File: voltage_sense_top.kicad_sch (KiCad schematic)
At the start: 46 parts, among them IC1 DAC101C081CIMK_NOPB, J1 Conn_Coaxial, J2 Conn_01x04, J4 HDMI_A, J5 Conn_Coaxial, U1 OPA188xxDBV, U2 ADA4000-1, U3 OPA188xxDBV, U4 MCP4017T-103E_LT, U5 OPA1641

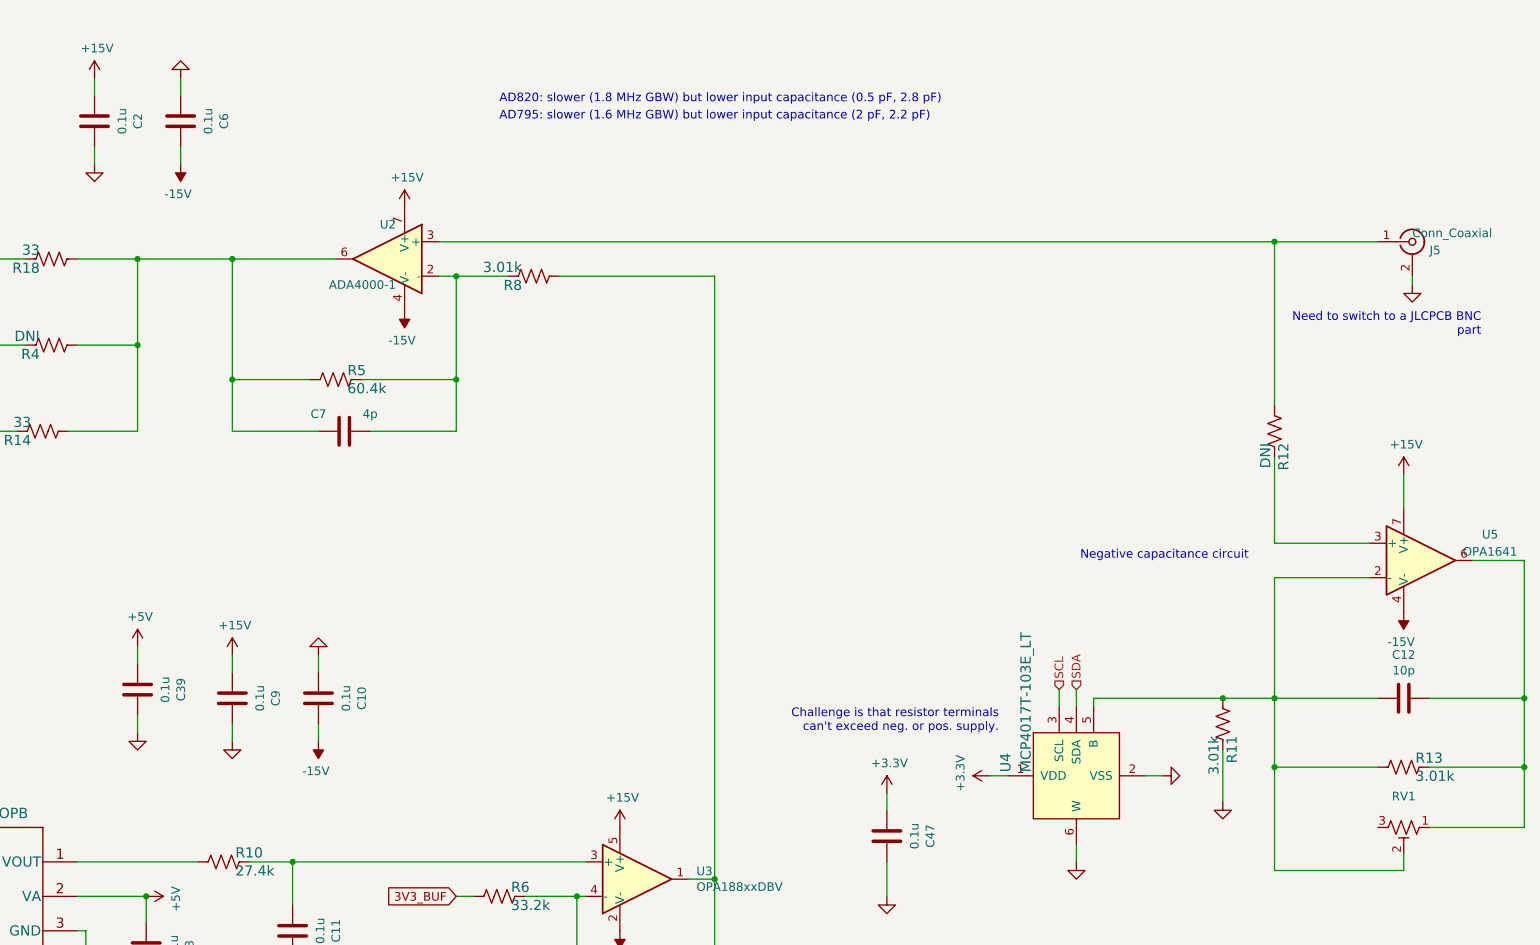
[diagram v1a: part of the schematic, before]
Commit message: moved SMA to same size as HDMI
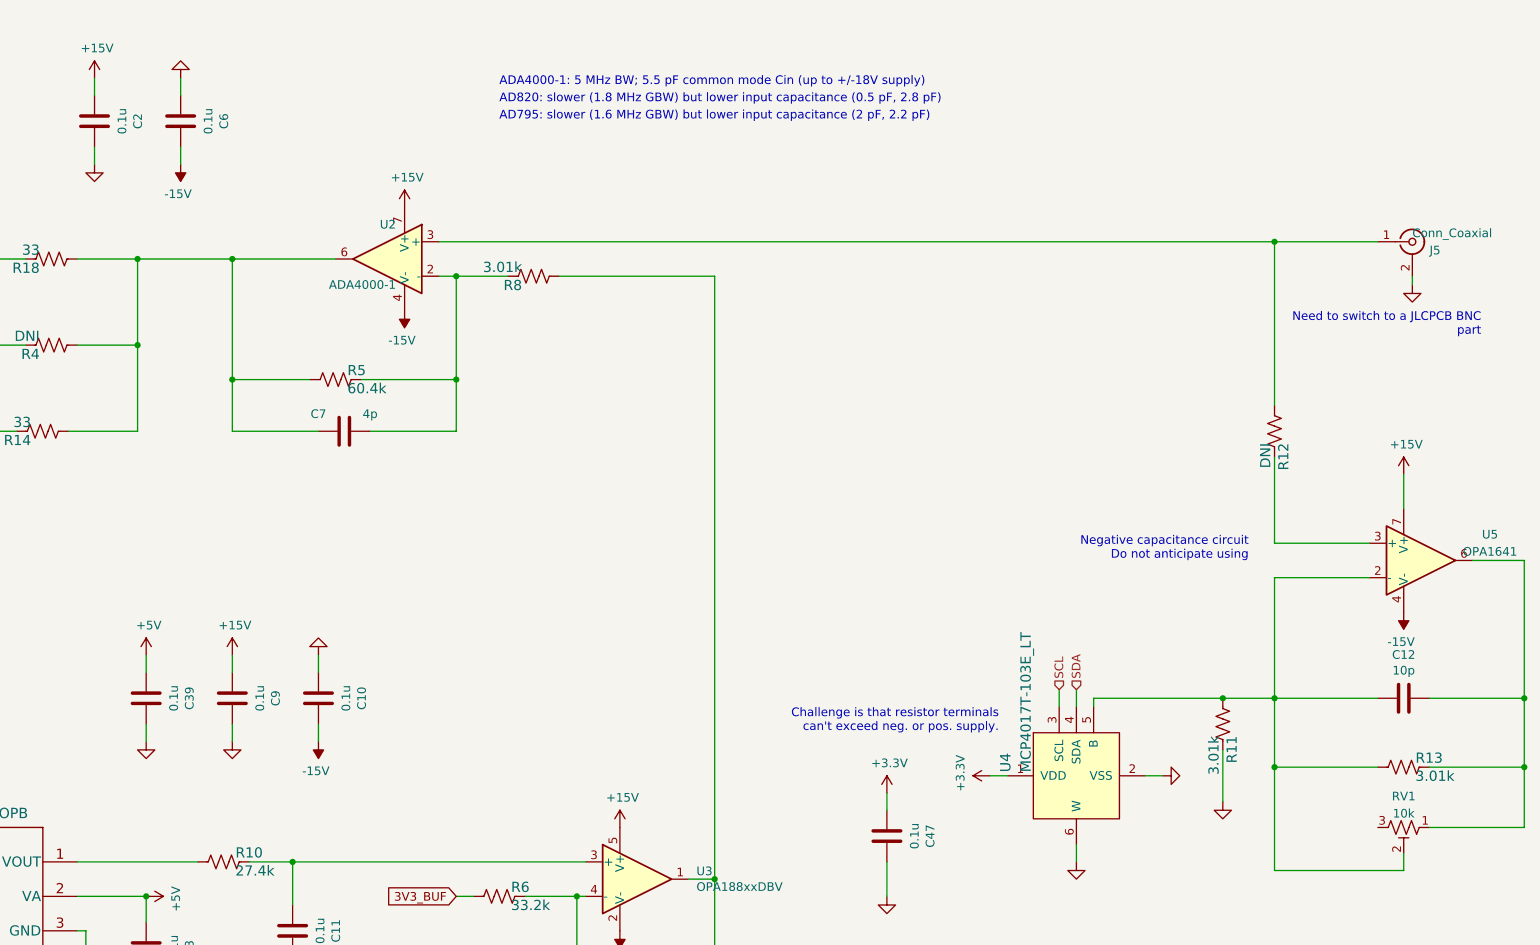
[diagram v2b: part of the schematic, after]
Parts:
- RV1: value (none) -> 10k; footprint (none) -> covg-kicad:Potentiometer_Nidec_ST-5ETW
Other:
- note added: "ADA4000-1: 5 MHz BW; 5.5 pF common mode Cin (up to +/-18V supply)"
- note added: "Negative capacitance circuit Do not anticipate using"
- note removed: "Negative capacitance circuit"
- moved on the sheet: C39
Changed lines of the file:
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@@
     (stroke (width 0) (type default) (color 0 0 0 0))
   )
-  (wire (pts (xy 199.39 119.38) (xy 199.39 116.84))
+  (wire (pts (xy 200.66 120.65) (xy 200.66 118.11))
     (stroke (width 0) (type default) (color 0 0 0 0))
   )
@@
     (stroke (width 0) (type default) (color 0 0 0 0))
   )
-  (wire (pts (xy 199.39 109.22) (xy 199.39 106.68))
+  (wire (pts (xy 200.66 110.49) (xy 200.66 107.95))
     (stroke (width 0) (type default) (color 0 0 0 0))
   )
@@
     (effects (font (size 1.27 1.27)) (justify left bottom))
   )
-  (text "Negative capacitance circuit" (at 363.22 93.98 180)
+  (text "Negative capacitance circuit\nDo not anticipate using"
+    (at 363.22 93.98 0)
     (effects (font (size 1.27 1.27)) (justify right bottom))
   )
@@
     (effects (font (size 1.27 1.27)) (justify right bottom))
   )
+  (text "ADA4000-1: 5 MHz BW; 5.5 pF common mode Cin (up to +/-18V supply) "
+    (at 252.73 24.13 0)
+    (effects (font (size 1.27 1.27)) (justify left bottom))
+  )
   (label "SDA" (at 140.97 148.59 0)
     (effects (font (size 1.27 1.27)) (justify left bottom))
@@
     (pin "2")
   )
-  (symbol (lib_id "Device:C") (at 199.39 113.03 180) (unit 1)
-    (in_bom yes) (on_board yes)
-    (property "Reference" "C39" (id 0) (at 205.7908 113.03 90))
-    (property "Value" "0.1u" (id 1) (at 203.4794 113.03 90))
-    (property "Footprint" "Capacitor_SMD:C_0603_1608Metric" (id 2) (at 198.4248 109.22 0)
-      (effects (font (size 1.27 1.27)) hide)
-    )
-    (property "Datasheet" "~" (id 3) (at 199.39 113.03 0)
-      (effects (font (size 1.27 1.27)) hide)
-    )
-    (property "Manf#" "CC0603MRX7R8BB104" (id 4) (at 205.7908 115.57 0)
-      (effects (font (size 1.27 1.27)) hide)
-    )
-    (property "Tolerance" "20%" (id 5) (at 205.7908 115.57 0)
-      (effects (font (size 1.27 1.27)) hide)
-    )
-    (property "voltage" "25V" (id 6) (at 205.7908 115.57 0)
-      (effects (font (size 1.27 1.27)) hide)
-    )
-    (pin "1")
-    (pin "2")
-  )
-  (symbol (lib_id "power:GND") (at 199.39 119.38 0) (unit 1)
-    (in_bom yes) (on_board yes)
-    (property "Reference" "#PWR0184" (id 0) (at 199.39 125.73 0)
-      (effects (font (size 1.27 1.27)) hide)
-    )
-    (property "Value" "GND" (id 1) (at 199.517 122.6312 90)
+  (symbol (lib_id "Device:C") (at 200.66 114.3 180) (unit 1)
+    (in_bom yes) (on_board yes)
+    (property "Reference" "C39" (id 0) (at 207.0608 114.3 90))
+    (property "Value" "0.1u" (id 1) (at 204.7494 114.3 90))
+    (property "Footprint" "Capacitor_SMD:C_0603_1608Metric" (id 2) (at 199.6948 110.49 0)
+      (effects (font (size 1.27 1.27)) hide)
+    )
+    (property "Datasheet" "~" (id 3) (at 200.66 114.3 0)
+      (effects (font (size 1.27 1.27)) hide)
+    )
+    (property "Manf#" "CC0603MRX7R8BB104" (id 4) (at 207.0608 116.84 0)
+      (effects (font (size 1.27 1.27)) hide)
+    )
+    (property "Tolerance" "20%" (id 5) (at 207.0608 116.84 0)
+      (effects (font (size 1.27 1.27)) hide)
+    )
+    (property "voltage" "25V" (id 6) (at 207.0608 116.84 0)
+      (effects (font (size 1.27 1.27)) hide)
+    )
+    (pin "1")
+    (pin "2")
+  )
+  (symbol (lib_id "power:GND") (at 200.66 120.65 0) (unit 1)
+    (in_bom yes) (on_board yes)
+    (property "Reference" "#PWR0184" (id 0) (at 200.66 127 0)
+      (effects (font (size 1.27 1.27)) hide)
+    )
+    (property "Value" "GND" (id 1) (at 200.787 123.9012 90)
       (effects (font (size 1.27 1.27)) (justify right) hide)
     )
-    (property "Footprint" "" (id 2) (at 199.39 119.38 0)
-      (effects (font (size 1.27 1.27)) hide)
-    )
-    (property "Datasheet" "" (id 3) (at 199.39 119.38 0)
-      (effects (font (size 1.27 1.27)) hide)
-    )
-    (pin "1")
-  )
-  (symbol (lib_id "power:+5V") (at 199.39 106.68 0) (unit 1)
-    (in_bom yes) (on_board yes)
-    (property "Reference" "#PWR0186" (id 0) (at 199.39 110.49 0)
-      (effects (font (size 1.27 1.27)) hide)
-    )
-    (property "Value" "+5V" (id 1) (at 199.771 102.2858 0))
-    (property "Footprint" "" (id 2) (at 199.39 106.68 0)
-      (effects (font (size 1.27 1.27)) hide)
-    )
-    (property "Datasheet" "" (id 3) (at 199.39 106.68 0)
+    (property "Footprint" "" (id 2) (at 200.66 120.65 0)
+      (effects (font (size 1.27 1.27)) hide)
+    )
+    (property "Datasheet" "" (id 3) (at 200.66 120.65 0)
+      (effects (font (size 1.27 1.27)) hide)
+    )
+    (pin "1")
+  )
+  (symbol (lib_id "power:+5V") (at 200.66 107.95 0) (unit 1)
+    (in_bom yes) (on_board yes)
+    (property "Reference" "#PWR0186" (id 0) (at 200.66 111.76 0)
+      (effects (font (size 1.27 1.27)) hide)
+    )
+    (property "Value" "+5V" (id 1) (at 201.041 103.5558 0))
+    (property "Footprint" "" (id 2) (at 200.66 107.95 0)
+      (effects (font (size 1.27 1.27)) hide)
+    )
+    (property "Datasheet" "" (id 3) (at 200.66 107.95 0)
       (effects (font (size 1.27 1.27)) hide)
     )
@@
     (in_bom yes) (on_board yes) (fields_autoplaced)
     (property "Reference" "RV1" (id 0) (at 386.08 128.7612 90))
-    (property "Value" "" (id 1) (at 386.08 131.2981 90))
-    (property "Footprint" "" (id 2) (at 386.08 133.35 0)
-      (effects (font (size 1.27 1.27)) hide)
-    )
+    (property "Value" "10k" (id 1) (at 386.08 131.2981 90))
+    (property "Footprint" "covg-kicad:Potentiometer_Nidec_ST-5ETW" (id 2) (at 386.08 133.35 0)
+      (effects (font (size 1.27 1.27)) hide)
+    )

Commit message: Add files via upload
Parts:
- removed R7: 27.4k, Resistor_SMD:R_0603_1608Metric, symbol Device:R_US
- removed U2: ADA4000-1, Package_SO:SOIC-8_3.9x4.9mm_P1.27mm, symbol covg-kicad:OPA828
- added C14, C15: 0.1u, Capacitor_SMD:C_0603_1608Metric, symbol Device:C
- added C21: 10p, Capacitor_SMD:C_0603_1608Metric, symbol Device:C
- added C24: 1u, Capacitor_SMD:C_0603_1608Metric, symbol Device:C
- added R17, R19, R20, R21, R22, R23, R24, R25: 100k, Resistor_SMD:R_0603_1608Metric, symbol Device:R_US
- added R26, R30: 3.01k, Resistor_SMD:R_0603_1608Metric, symbol Device:R_US
- added R27, R28: 10k, Resistor_SMD:R_0603_1608Metric, symbol Device:R_US
- added R29: 4.99k, Resistor_SMD:R_0603_1608Metric, symbol Device:R_US
- added R31: 49.9, Resistor_SMD:R_0603_1608Metric, symbol Device:R_US
- added U2: TCA9555DBR, Package_SO:SSOP-24_5.3x8.2mm_P0.65mm, symbol Interface_Expansion:TCA9555DBR
- added U7: ADA4000-2ARZ-R7, covg-kicad:R_8_ADI, symbol ADA4000-2:ADA4000-2ARZ-R7
- C11: value 0.1u -> 1u; Manf# CC0603MRX7R8BB104 -> CC0603KRX7R7BB105
- C12: Manf# (none) -> CC0603JRNPO8BN100
- C7: value 4p -> 0.1u; Manf# CC0603CRNPO9BN4R0 -> CC0603MRX7R8BB104; Tolerance 20% -> (none)
- C8: value 0.1u -> 1n; Manf# CC0603MRX7R8BB104 -> CC0603KRX7R8BB102
- J1: footprint covg-kicad:SMA_HJ_SMA788 -> covg-kicad:BU-SMA-G; Manf# (none) -> C2874827
- J2: value Conn_01x04 -> DNI
- J5: Manf# (none) -> C2874827
- R10: value 27.4k -> 49.9k; Manf# RC0603FR-0727K4L -> RT0603BRB0749K9L
- R11: Manf# RC0603FR-073k01L -> RC0603JR-070RL
- R12: value DNI -> 0
- R14: Manf# (none) -> RC0603FR-0733RL
- R15, R2: Manf# (none) -> RC0603FR-0730KL
- R5: value 60.4k -> 100k; Manf# RC0603FR-0760k4L -> RC0603FR-07100KL
- R6: value 33.2k -> 49.9k; Manf# RC0603FR-0733K2L -> RT0603BRB0749K9L
- R8: value 3.01k -> DNI; Manf# RC0603FR-073k01L -> RC0603FR-07100KL
- R9: value 10k -> 4.99k; Manf# RC0603FR-0710KL -> RT0603BRB074K99L
- RV1: footprint covg-kicad:Potentiometer_Nidec_ST-5ETW -> covg-kicad:TRIM_3269W-1-103GLF
- U5: Manf# (none) -> OPA1641AIDR
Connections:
- net +15V: now also C14.2, U7.8 (V+)
- net +3V3: now also C7.2, R5.1, U2.2 (A1), U2.24 (VCC), U2.3 (A2); no longer U1.3 (+)
- net +5V: no longer C3.2, IC1.2 (VA)
- net -15V: now also C15.1, U7.4 (-V)
- net AMP_OUT: now also R18.2; no longer R18.1
- net CAL_ADC: now also R4.2; no longer R4.1
- net GND: now also C7.1, R8.2, C14.1, C15.2, C24.1, R17.2, R19.2, R20.2, R21.2, R22.2, R23.2, R24.2, R25.2, R26.1, R28.2, R29.1, U2.12 (GND)
- net SCL: now also U2.22 (SCL)
- net SDA: now also U2.23 (SDA)
- net at R11.2, R13.2, RV1.2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: no longer C12.2
- net at R12.1, U5.3 (+): now also C12.2
- net OFF_ADJ: now reaches R9.1, U3.1
- net OFF_ADJ: now also C21.1, R31.2; no longer C8.2, R8.2
- net at C11.2, R10.1, U3.3 (+): now also R29.2
- net at R6.1, R9.2, U3.4 (-): now also C21.2
- net at J5.1 (In), R12.2: now also U7.5 (+INB)
- net 3V3_BUF renamed 2V_BUF
- new net: C8.2, R30.2, R31.1
- new net: R5.2, R8.1, U2.21 (A0)
- new net: C24.2, R27.1, R28.1, U1.3 (+)
- new net +4V: C3.2, IC1.2 (VA), R27.2
- new net -IN_A: R26.2, U7.2 (-INA)
- new net -IN_B: R30.1, U7.6 (-INB)
- new net STG1_OUT: R18.1, R4.1, U7.3 (+INA), U7.7 (OUTB)
- new net SW0: R17.1, U2.4 (P00)
- new net SW1: R20.1, U2.5 (P01)
- new net SW2: R22.1, U2.6 (P02)
- new net SW3: R24.1, U2.7 (P03)
- new net SW4: R19.1, U2.8 (P04)
- new net SW5: R21.1, U2.9 (P05)
- new net SW6: R23.1, U2.10 (P06)
- new net SW7: R25.1, U2.11 (P07)
- new net gain_adjust_2/OUT: R14.2, U7.1 (OUTA)
- no-connect marks 0 -> 11
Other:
- added sheet gain_adjust_1 (gain_adjust.kicad_sch)
- added sheet gain_adjust_2 (gain_adjust.kicad_sch)
- note added: "0x27 = 7b0100111 7b0100 A2 A1 A0"
- note added: "0x2F = 7b0101111"
- note added: "3b110"
- note added: "4.096V VDAC -> OFF_ADJ = 200mV 0V VDAC -> OFF_ADJ = -200mV Approx. 0.4mV resolution per DAC bit"
- note added: "Negative capacitance circuit lowers rise time"
- note added: "OFF_ADJ = (R9/R6)*(VDAC-2V_BUF) OFF_ADJ = 0.10*(VDAC-2V_BUF)"
- note added: "See Figures 41 & 42 on datasheet For C8/R31 value"
- note added: "dual ADA4000 amp"
- note removed: "Negative capacitance circuit Do not anticipate using"
- note removed: "OFF_ADJ = (VDAC*(1/R50 + 1/R48 + 1/R47)- 3.3/R47)*R50 OFF_ADJ = VDAC*1.6662 - 0.9940"
- moved on the sheet: C1, C10, C11, C12, C13, C2, C3, C31, C32, C39, C47, C6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

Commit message: All production files in jlcpcb/production_files
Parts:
- J5: value Conn_Coaxial -> (none); footprint Connector_Coaxial:BNC_Amphenol_B6252HB-NPP3G-50_Horizontal -> (none); Manf# C2874827 -> (none)
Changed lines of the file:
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@@
   )
   (text "Challenge is that resistor \nterminals can't exceed neg. \nor pos. supply."
-    (at 325.755 116.205 180)
+    (at 325.755 116.205 0)
     (effects (font (size 1.27 1.27)) (justify right bottom))
   )
@@
       (effects (font (size 1.27 1.27)) (justify left))
     )
-    (property "Value" "Conn_Coaxial" (id 1) (at 387.985 48.895 0)
+    (property "Value" "" (id 1) (at 387.985 48.895 0)
       (effects (font (size 1.27 1.27)) (justify left))
     )
-    (property "Footprint" "Connector_Coaxial:BNC_Amphenol_B6252HB-NPP3G-50_Horizontal" (id 2) (at 387.985 50.165 0)
+    (property "Footprint" "" (id 2) (at 387.985 50.165 0)
       (effects (font (size 1.27 1.27)) hide)
     )
@@
       (effects (font (size 1.27 1.27)) hide)
     )
-    (property "Manf#" "C2874827" (id 4) (at 387.985 50.165 90)
-      (effects (font (size 1.27 1.27)) hide)
-    )
+    (property "Manf#" "" (id 4) (at 387.985 50.165 90)
+      (effects (font (size 1.27 1.27)) hide)
+    )

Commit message: add modified production files; schematic update by KiCAD version to 8.0.1
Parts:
- J5: value (none) -> DNI; footprint (none) -> Connector_Coaxial:BNC_Amphenol_B6252HB-NPP3G-50_Horizontal
